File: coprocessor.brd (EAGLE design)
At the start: 33 x 53.3 mm, 50 parts, among them IC1 MEGA32U2, U1 TPS61090RSAR, U3 V_REG_LDOSMD2, U4 AZV321, U5 MCP48, U6 16MHZ, U7 CBT3244AD

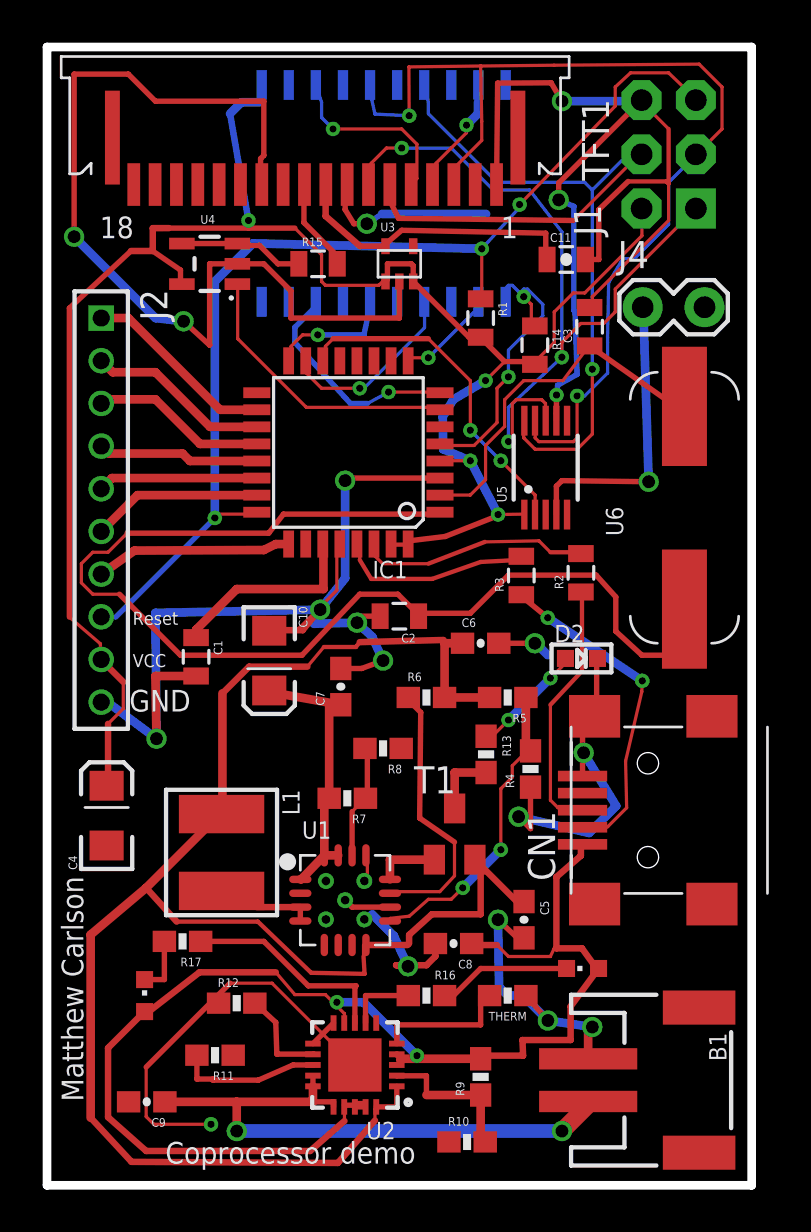
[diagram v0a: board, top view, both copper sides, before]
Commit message: redid the inductor to save some space
I noticed that I setup the charging circuit incorrectly
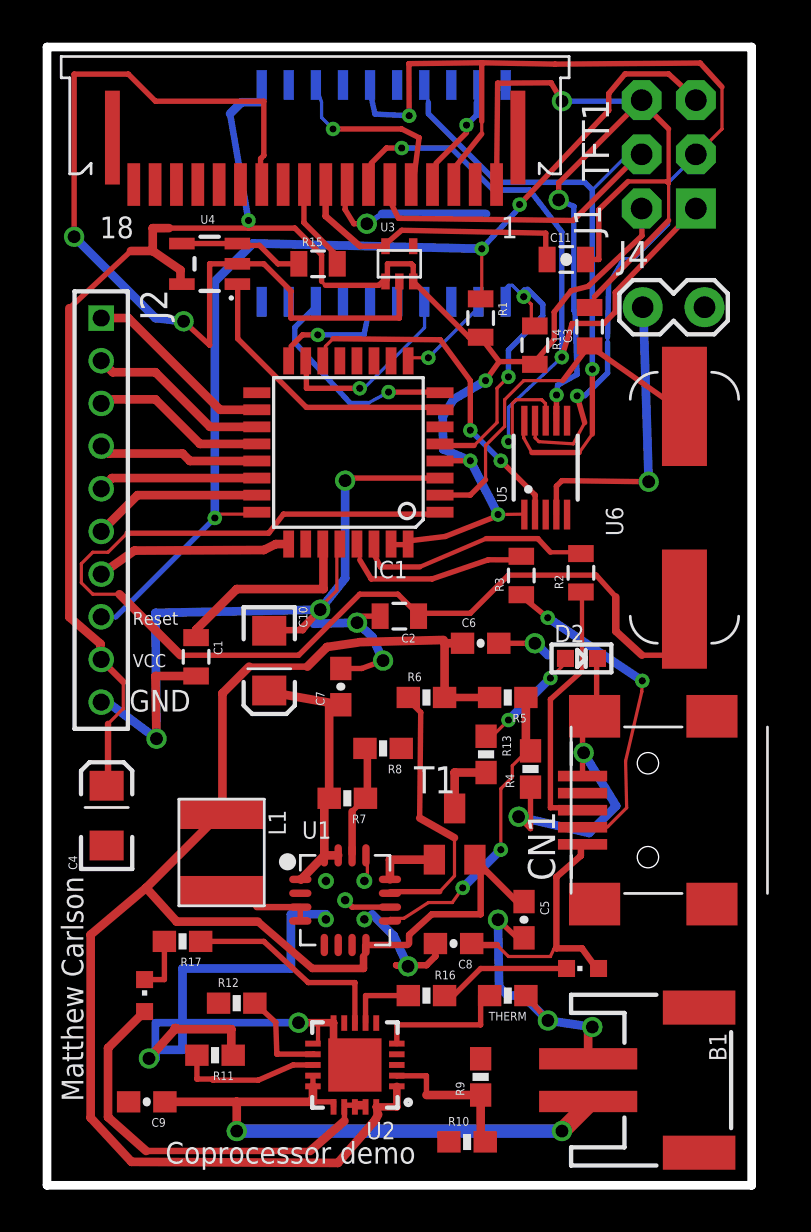
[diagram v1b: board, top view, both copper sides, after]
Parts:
- L1: device custom:MICROBUILDER_INDUCTOR_5X5MM_NR5040_NOTHERMALS -> custom:MICROBUILDER_INDUCTOR_4.9X4.9MM
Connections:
- new net N$31: LED2.A
- new net N$32: LED1.A
- new net N$33: U2.P$18, U2.P$19
- net VCC: now also U2.P$17, U2.P$3, U2.P$4, U2.P$9
- net V_USB: no longer LED1.A, LED2.A, R9.2, U2.P$17, U2.P$18, U2.P$19, U2.P$3, U2.P$4, U2.P$9
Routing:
- net V_USB: track 61.8 -> 12.2 mm, vias 2 -> 0
- net N$31: track 0.00 -> 18.4 mm
- net GND: track 214.6 -> 229.8 mm, vias 19 -> 20
- net N$33: track 0.00 -> 1.08 mm
- net V_BATT: track 82.7 -> 82.2 mm

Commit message: had to just completely revamp the voltages
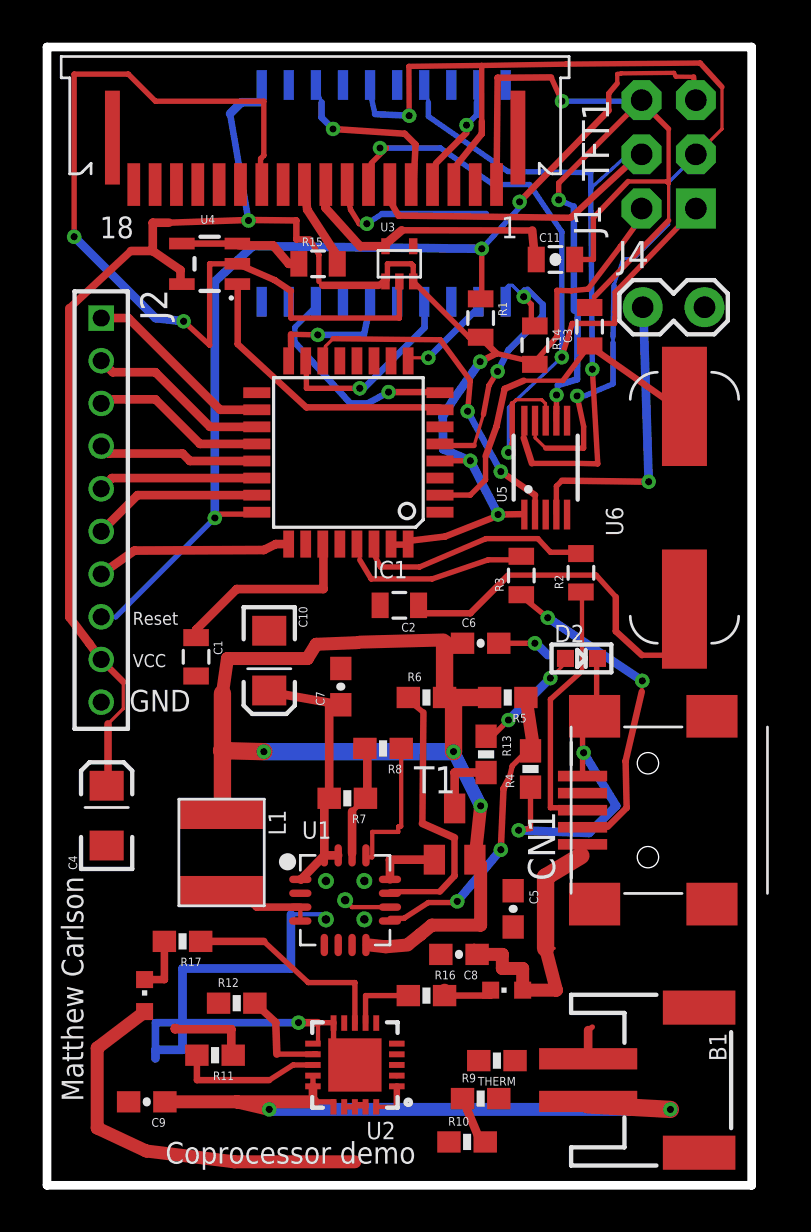
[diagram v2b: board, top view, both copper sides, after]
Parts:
- moved LED1 3.70 mm to (21.5, 9.14)
- moved THERM 3.09 mm to (21.1, 5.84)
- moved R9 1.02 mm to (20.3, 4.06), turned to 0 degrees
- moved C5 0.72 mm to (21.8, 13.0)
- moved C8 0.57 mm to (19.3, 10.8)
- moved C11 0.51 mm to (23.8, 43.4)
- moved C2 0.51 mm to (16.5, 27.2)
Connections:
- net N$4 renamed PWR_ENABLE
- net N$8 renamed VLIPO
- removed net N$31: LED2.A
- removed net N$32: LED1.A
- removed net N$33: U2.P$18, U2.P$19
- net VCC: no longer U2.P$17, U2.P$3, U2.P$4, U2.P$9
- net V_USB: now also LED1.A, LED2.A, R9.2, U2.P$17, U2.P$18, U2.P$19, U2.P$3, U2.P$4, U2.P$9
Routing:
- net GND: track 229.8 -> 165.6 mm, vias 20 -> 10
- net N$9: track 55.4 -> 18.4 mm
- net V_BATT: track 82.2 -> 54.8 mm, vias 0 -> 3
- net V_USB: track 12.2 -> 34.3 mm
- net N$31: track 18.4 -> 0.00 mm
- net N$24: track 6.60 -> 0.00 mm
- net VLIPO: track 27.9 -> 33.7 mm
- net N$1: track 7.25 -> 2.43 mm
- net N$22: track 6.24 -> 2.67 mm
- net MISO: track 37.6 -> 39.4 mm
- net MOSI: track 44.2 -> 45.8 mm
- net VCC: track 90.6 -> 91.7 mm
- net N$33: track 1.08 -> 0.00 mm
- net RESET: track 50.7 -> 51.5 mm
- net SCK: track 49.6 -> 50.3 mm
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
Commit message: added an SVG logo and redid the gerbers
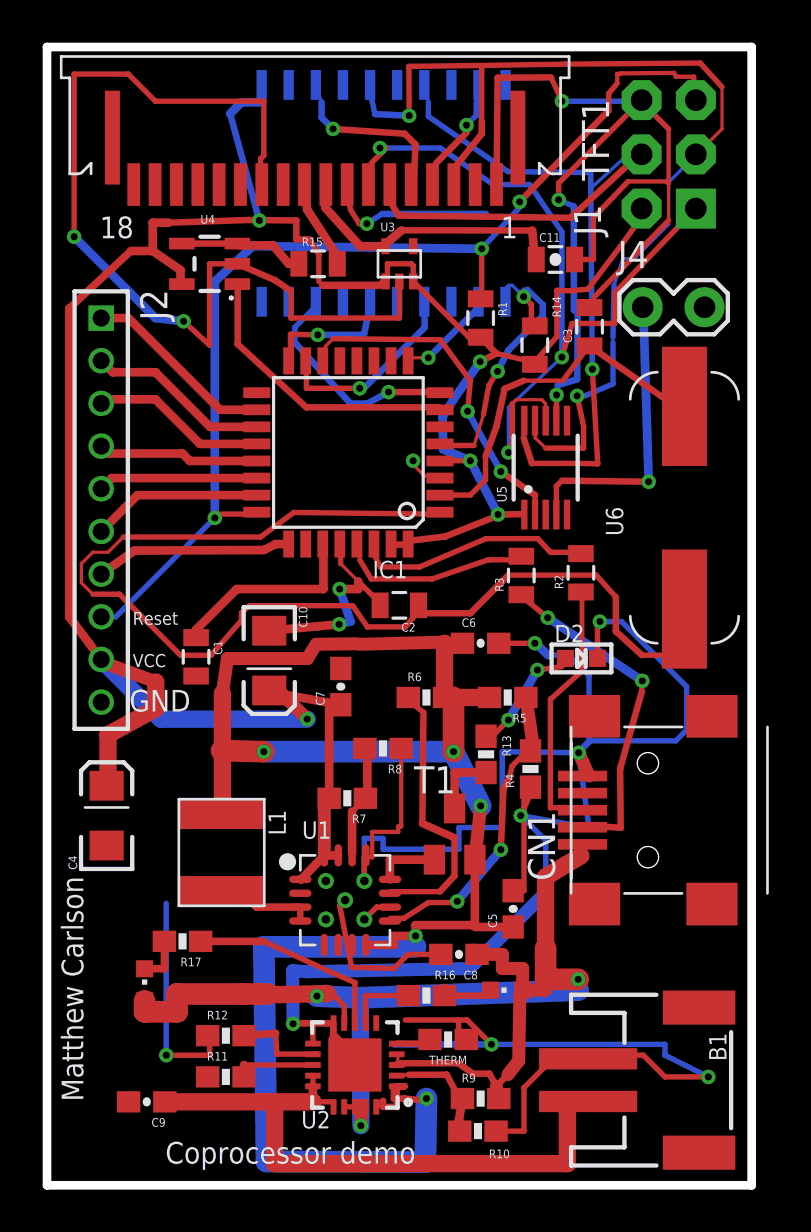
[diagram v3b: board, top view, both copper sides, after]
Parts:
- moved THERM 2.49 mm to (18.8, 6.83)
- moved R12 1.61 mm to (8.38, 7.01)
- moved R11 1.14 mm to (8.38, 5.08), turned to 0 degrees
- moved R10 0.72 mm to (20.2, 2.54), turned to 180 degrees
- moved LED2 0.51 mm to (4.57, 9.40)
- turned C5 to 90 degrees
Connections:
- removed net 5V: C10.A, C7.1, R7.2, U1.1, U1.15, U1.16
- net VCC: now also C10.A, C7.1, R7.2, U1.1, U1.15, U1.16
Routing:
- net GND: track 165.6 -> 268.7 mm, vias 10 -> 17
- net N$9: track 18.4 -> 56.2 mm
- net V_BATT: track 54.8 -> 88.4 mm, vias 3 -> 5
- net VCC: track 91.7 -> 122.3 mm, vias 4 -> 5
- net V_USB: track 34.3 -> 62.9 mm, vias 0 -> 3
- net 5V: track 14.2 -> 0.00 mm
- net VLIPO: track 33.7 -> 30.0 mm, vias 2 -> 0
- net N$12: track 6.81 -> 3.79 mm
- net N$1: track 2.43 -> 5.28 mm
- net N$24: track 0.00 -> 2.13 mm
- net N$23: track 2.72 -> 2.21 mm

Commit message: added new gerbers and ordered the board
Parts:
- removed U$4: (no value), custom:LOGO_1INCH
- added U$2: LOGO2INCH_SVG, custom:LOGO_2INCH_SVG
- moved LOGO1 25.0 mm to (30.6, 3.00)
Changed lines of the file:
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@@
 <text x="6.731" y="23.2156" size="1.016" layer="21" distance="34" rot="R180">GND</text>
 <text x="0.6858" y="14.478" size="1.016" layer="21" font="vector" ratio="10" rot="R270">Matthew Carlson</text>
-<text x="1.27" y="1.27" size="1.016" layer="22" font="vector" ratio="10" rot="MR90">January 2017</text>
+<text x="30.226" y="5.842" size="1.016" layer="22" font="vector" ratio="10" rot="MR90">January 2017</text>
 <text x="17.272" y="2.032" size="1.016" layer="21" font="vector" ratio="13" rot="R180">Coprocessor demo</text>
 <text x="4.0132" y="24.2824" size="0.6096" layer="25">VCC</text>
@@
 </element>
 <element name="B1" library="custom" package="MICROBUILDER_JSTPH2" value="" x="29.0576" y="4.9276" rot="R270"/>
-<element name="LOGO1" library="SparkFun-Aesthetics" package="OSHW-LOGO-S" value="OSHW-LOGOS" x="28.6004" y="27.8892" rot="MR90"/>
+<element name="LOGO1" library="SparkFun-Aesthetics" package="OSHW-LOGO-S" value="OSHW-LOGOS" x="30.6324" y="2.9972" rot="MR90"/>
 <element name="C9" library="SparkFun-Capacitors" package="0603-CAP" value="10uF" x="4.6736" y="3.9116" rot="R180">
 <attribute name="PROD_ID" value="CAP-11015" x="4.6736" y="3.9116" size="1.778" layer="27" rot="R180" display="off"/>
@@
 </element>
 <element name="THERM" library="SparkFun-Resistors" package="0603-RES" value="16k" x="18.796" y="6.8326" rot="R180"/>
-<element name="U$4" library="custom" package="LOGO_1INCH" value="" x="25.9588" y="0.762" rot="MR90"/>
+<element name="U$2" library="custom" package="LOGO_2INCH_SVG" value="LOGO2INCH_SVG" x="0.508" y="2.032" rot="MR90"/>
 </elements>
 <signals>
@@
 <contactref element="R1" pad="1"/>
 <contactref element="J2" pad="8"/>
-<wire x1="8.0415" y1="31.4512" x2="9.8285" y2="31.4512" width="0.254" layer="1"/>
+<wire x1="8.0415" y1="31.4512" x2="9.8285" y2="31.4512" width="0.3048" layer="1"/>
 <wire x1="7.8628" y1="31.2725" x2="8.0415" y2="31.4512" width="0.1524" layer="1"/>
-<wire x1="3.2166" y1="26.6263" x2="7.8628" y2="31.2725" width="0.254" layer="16"/>
+<wire x1="3.2166" y1="26.6263" x2="7.8628" y2="31.2725" width="0.3048" layer="16"/>
 <wire x1="2.6805" y1="26.6263" x2="3.2166" y2="26.6263" width="0.1524" layer="16"/>
 <wire x1="9.8285" y1="31.4512" x2="9.8298" y2="31.5408" width="0.1524" layer="1"/>
@@
 <wire x1="22.8736" y1="38.5992" x2="22.86" y2="38.47" width="0.1524" layer="1"/>
 <wire x1="1.9938" y1="25.3754" x2="2.5018" y2="24.6606" width="0.4064" layer="1"/>
-<wire x1="1.0477" y1="26.6263" x2="1.9938" y2="25.3754" width="0.4064" layer="1"/>
-<wire x1="1.0477" y1="41.101" x2="1.0477" y2="26.6263" width="0.4064" layer="1"/>
-<wire x1="3.9314" y1="43.7815" x2="1.0477" y2="41.101" width="0.3556" layer="1"/>
-<wire x1="4.9546" y1="43.7815" x2="3.9314" y2="43.7815" width="0.4064" layer="1"/>
+<wire x1="1.0477" y1="26.6263" x2="1.9938" y2="25.3754" width="0.6096" layer="1"/>
+<wire x1="1.0477" y1="42.117" x2="1.0477" y2="26.6263" width="0.508" layer="1"/>
+<wire x1="3.9314" y1="43.7815" x2="1.0477" y2="42.117" width="0.6096" layer="1"/>
+<wire x1="4.9546" y1="43.7815" x2="3.9314" y2="43.7815" width="0.6096" layer="1"/>
 <wire x1="2.5018" y1="24.6606" x2="2.54" y2="24.64" width="0.1524" layer="1"/>
 <wire x1="18.5657" y1="34.4891" x2="19.8357" y2="33.953" width="0.4064" layer="16"/>
